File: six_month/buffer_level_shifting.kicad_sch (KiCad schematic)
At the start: 7 parts, among them U3 TCA4307DGKR

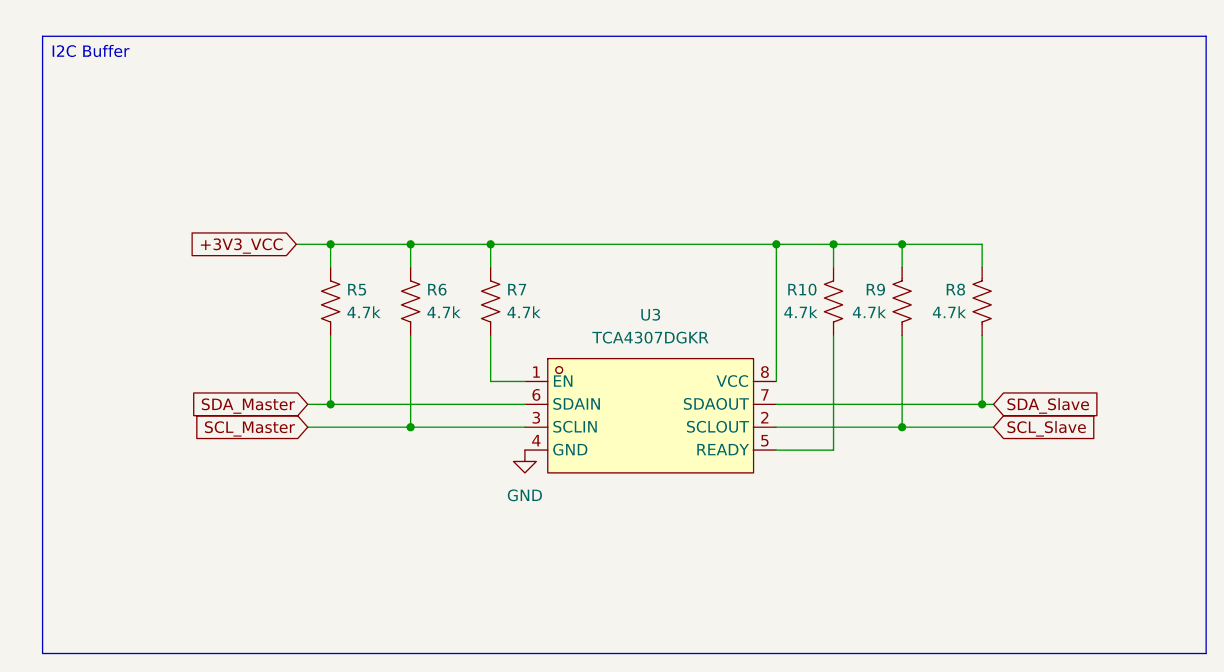
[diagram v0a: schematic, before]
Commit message: Changes
Removed the microphone idea, added a DAC for Bluetooth to Line out. Allows for external speakers to be connected via an Aux cable
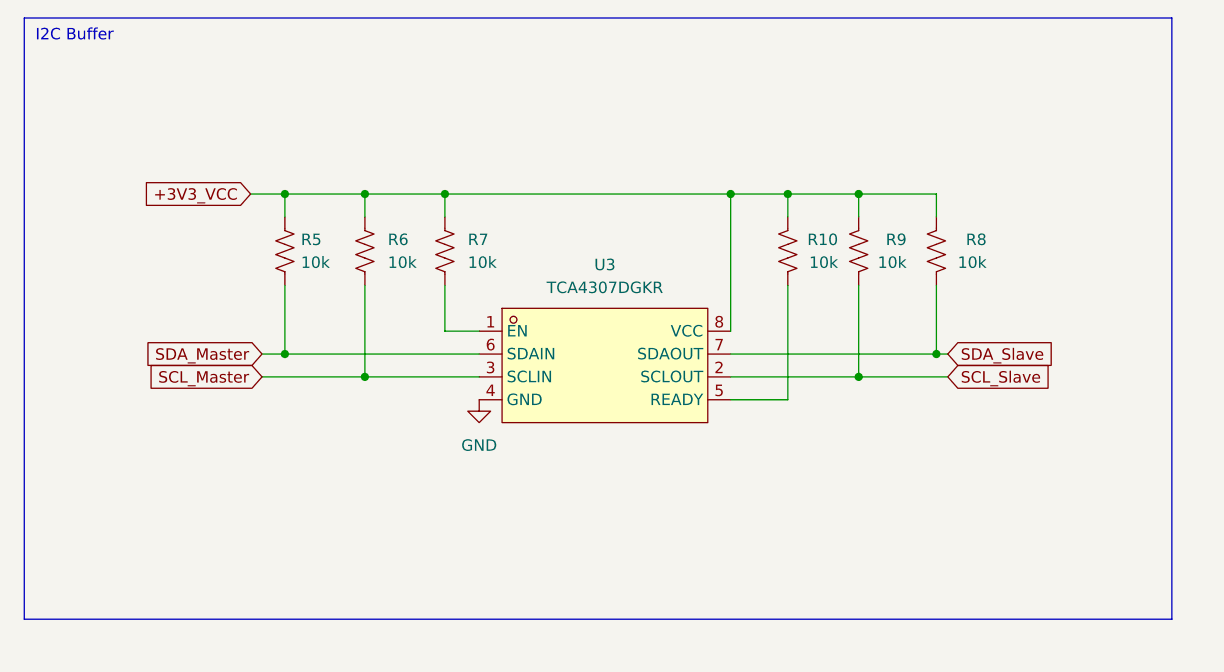
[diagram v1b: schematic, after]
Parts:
- R10, R5, R6, R7, R8, R9: value 4.7k -> 10k
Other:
- note added: "I2C Buffer"
- moved on the sheet: R10, R5, R6, R7, R8, R9, U3
